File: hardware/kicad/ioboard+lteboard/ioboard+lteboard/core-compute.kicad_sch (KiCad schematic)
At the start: 14 parts, among them J7 USB_C_Receptacle_USB2.0_14P, J8 Amphenol_132163, SW1 SW_Push, SW2 SW_Push, U17 ESP32-S3-WROOM-1U

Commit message: Step 6: pin assignment and wiring on ioboard+lteboard
- core-compute: fix USB D+/D- to native GPIO19/GPIO20 (was on GPIO13/14)
- analog_io: expose ISO1540 logic-side I2C as hierarchical labels (bidirectional)
- core-compute: add 14 hierarchical labels for ethernet/lte/rs485/rs232 pin assignment
- root sheet: wire all 14 signals to their subsystems, confirm I2C 3-way merge
  (analog_io + core-compute + status_indication)
- root sheet: VBAT_LTE tied power<->lte (casual, ahead of the formal
  board-to-board connector decision, which stays a step 7 item; 3V3_LOGIC
  intentionally left split for the same reason)
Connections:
- net GND_LOGIC: now also R39.2; no longer R39.1
- net ETH_MISO: now reaches U17.21 (IO13)
- net ETH_MISO: no longer R40.1
- net at SW2.1: now also R39.1; no longer R39.2
- net ETH_INTN: now reaches U17.22 (IO14)
- net ETH_INTN: no longer R41.1
- net LTE_TXD: now reaches U17.10 (IO17)
- net LTE_RXD: now reaches U17.11 (IO18)
- net USB_D-: now reaches U17.13 (USB_D-)
- net USB_D-: now also R40.1
- net USB_D+: now reaches U17.14 (USB_D+)
- net USB_D+: now also R41.1
- net ETH_SCSN: now reaches U17.18 (IO10)
- net ETH_MOSI: now reaches U17.19 (IO11)
- net ETH_SCLK: now reaches U17.20 (IO12)
- net RS485_RXD: now reaches U17.38 (IO2)
- net RS485_TXD: now reaches U17.39 (IO1)
- net ETH_RSTN: now reaches U17.4 (IO4)
- net RS232_TXD: now reaches U17.5 (IO5)
- net RS232_RXD: now reaches U17.6 (IO6)
- net LTE_PWRKEY: now reaches U17.8 (IO15)
- net LTE_RESET: now reaches U17.9 (IO16)
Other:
- moved on the sheet: R39, R40, R41, SW2

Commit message: added missing hierarchical labels for core-compute, digitil_inputs and relay_output
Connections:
- net DI4_MCU: now reaches U17.15 (IO3)
- net DI7_MCU: now reaches U17.16 (IO46)
- net DI8_MCU: now reaches U17.24 (IO47)
- net DI3_MCU: now reaches U17.25 (IO48)
- net RELAY2_CTRL: now reaches U17.31 (IO38)
- net DI5_MCU: now reaches U17.32 (IO39)
- net DI1_MCU: now reaches U17.33 (IO40)
- net DI2_MCU: now reaches U17.34 (IO41)
- net DI6_MCU: now reaches U17.35 (IO42)
- net RELAY4_CTRL: now reaches U17.36 (RXD0)
- net RELAY3_CTRL: now reaches U17.37 (TXD0)
- net RELAY1_CTRL: now reaches U17.7 (IO7)
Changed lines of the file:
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@@
+		)
+	)
+	(hierarchical_label "DI7_MCU"
+		(shape input)
+		(at 144.78 100.33 0)
+		(effects
+			(font
+				(size 1.27 1.27)
+			)
+			(justify left)
 		)
 	)
@@
 		)
 	)
+	(hierarchical_label "DI6_MCU"
+		(shape input)
+		(at 144.78 95.25 0)
+		(effects
+			(font
+				(size 1.27 1.27)
+			)
+			(justify left)
+		)
+	)
+	(hierarchical_label "DI3_MCU"
+		(shape input)
+		(at 144.78 105.41 0)
+		(effects
+			(font
+				(size 1.27 1.27)
+			)
+			(justify left)
+		)
+	)
+	(hierarchical_label "RELAY4_CTRL"
+		(shape output)
+		(at 144.78 62.23 0)
+		(effects
+			(font
+				(size 1.27 1.27)
+			)
+			(justify left)
+		)
+	)
+	(hierarchical_label "DI8_MCU"
+		(shape input)
+		(at 144.78 102.87 0)
+		(effects
+			(font
+				(size 1.27 1.27)
+			)
+			(justify left)
+		)
+	)
+	(hierarchical_label "DI2_MCU"
+		(shape input)
+		(at 144.78 92.71 0)
+		(effects
+			(font
+				(size 1.27 1.27)
+			)
+			(justify left)
+		)
+	)
 	(hierarchical_label "LTE_RESET"
 		(shape output)
@@
 		)
 	)
+	(hierarchical_label "DI1_MCU"
+		(shape input)
+		(at 144.78 90.17 0)
+		(effects
+			(font
+				(size 1.27 1.27)
+			)
+			(justify left)
+		)
+	)
 	(hierarchical_label "ETH_RSTN"
 		(shape output)
@@
 		)
 	)
+	(hierarchical_label "RELAY2_CTRL"
+		(shape output)
+		(at 144.78 85.09 0)
+		(effects
+			(font
+				(size 1.27 1.27)
+			)
+			(justify left)
+		)
+	)
 	(hierarchical_label "ETH_SCSN"
 		(shape output)
@@
 		)
 	)
+	(hierarchical_label "DI5_MCU"
+		(shape input)
+		(at 144.78 87.63 0)
+		(effects
+			(font
+				(size 1.27 1.27)
+			)
+			(justify left)
+		)
+	)
 	(hierarchical_label "RS485_TXD"
 		(shape output)
@@
 		)
 	)
+	(hierarchical_label "DI4_MCU"
+		(shape input)
+		(at 114.3 72.39 180)
+		(effects
+			(font
+				(size 1.27 1.27)
+			)
+			(justify right)
+		)
+	)
 	(hierarchical_label "ETH_MOSI"
 		(shape output)
@@
 		)
 	)
+	(hierarchical_label "RELAY1_CTRL"
+		(shape output)
+		(at 114.3 82.55 180)
+		(effects
+			(font
+				(size 1.27 1.27)
+			)
+			(justify right)
+		)
+	)
 	(hierarchical_label "RS232_RXD"
 		(shape input)
@@
 		)
 	)
+	(hierarchical_label "RELAY3_CTRL"
+		(shape output)
+		(at 144.78 59.69 0)
+		(effects
+			(font
+				(size 1.27 1.27)
+			)
+			(justify left)
+		)
+	)

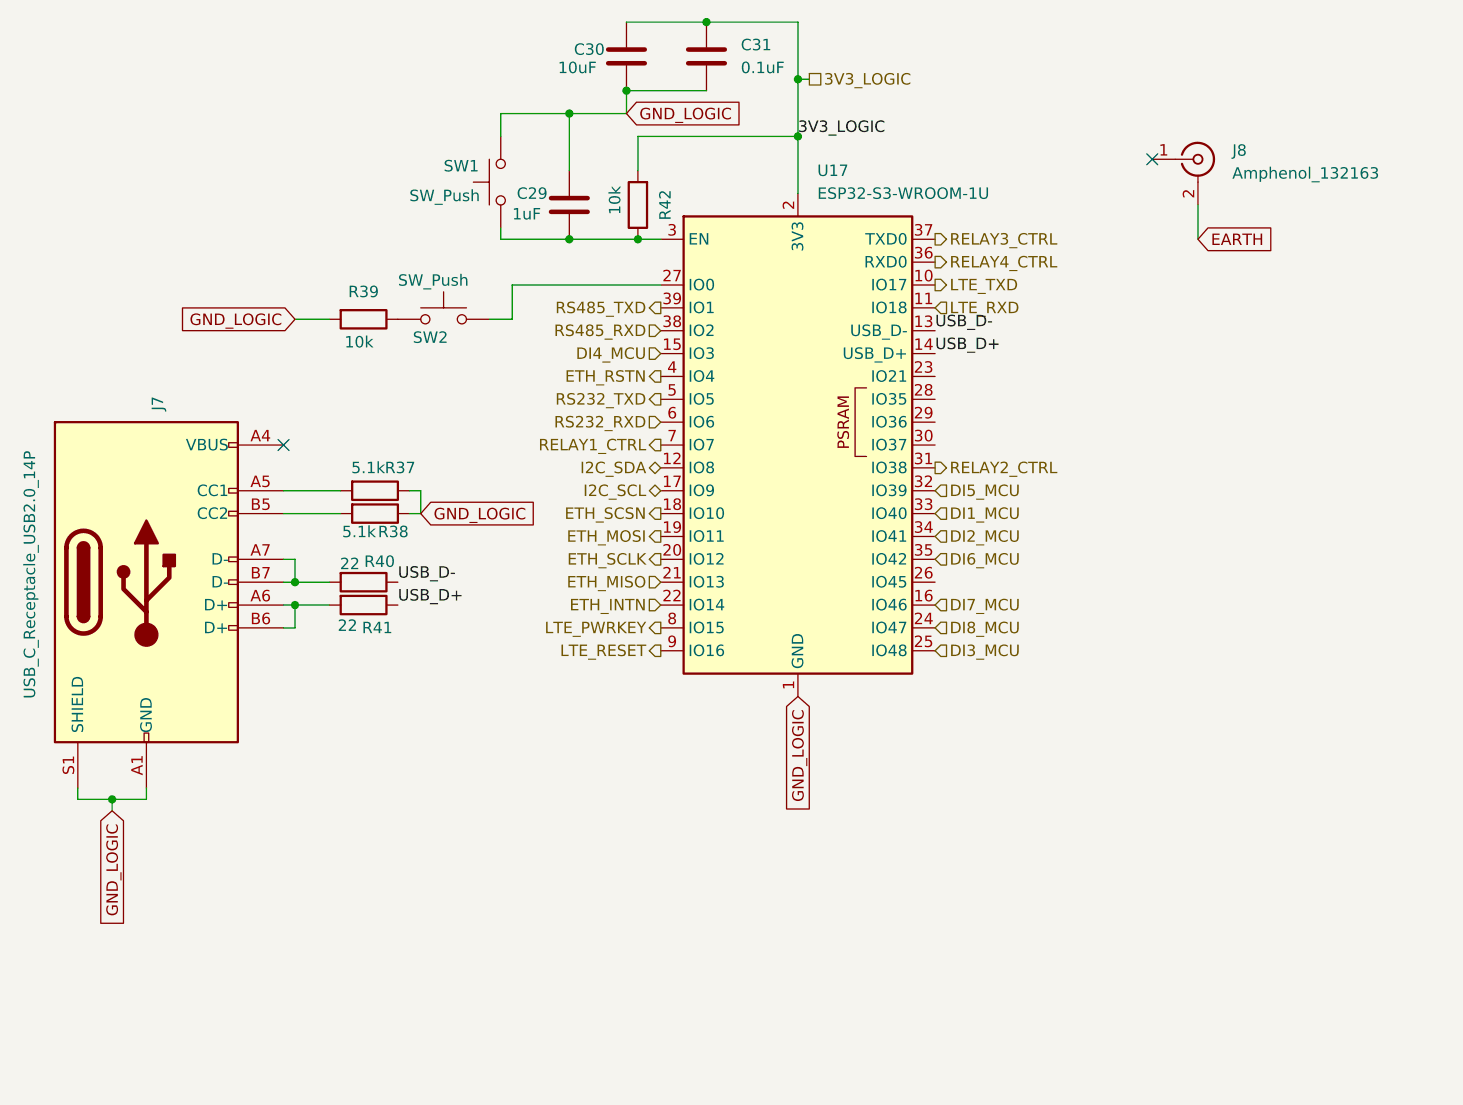
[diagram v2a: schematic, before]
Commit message: Close roadmap steps 6/7: pin assignment, board-to-board wiring, ERC pass clean; update docs to match
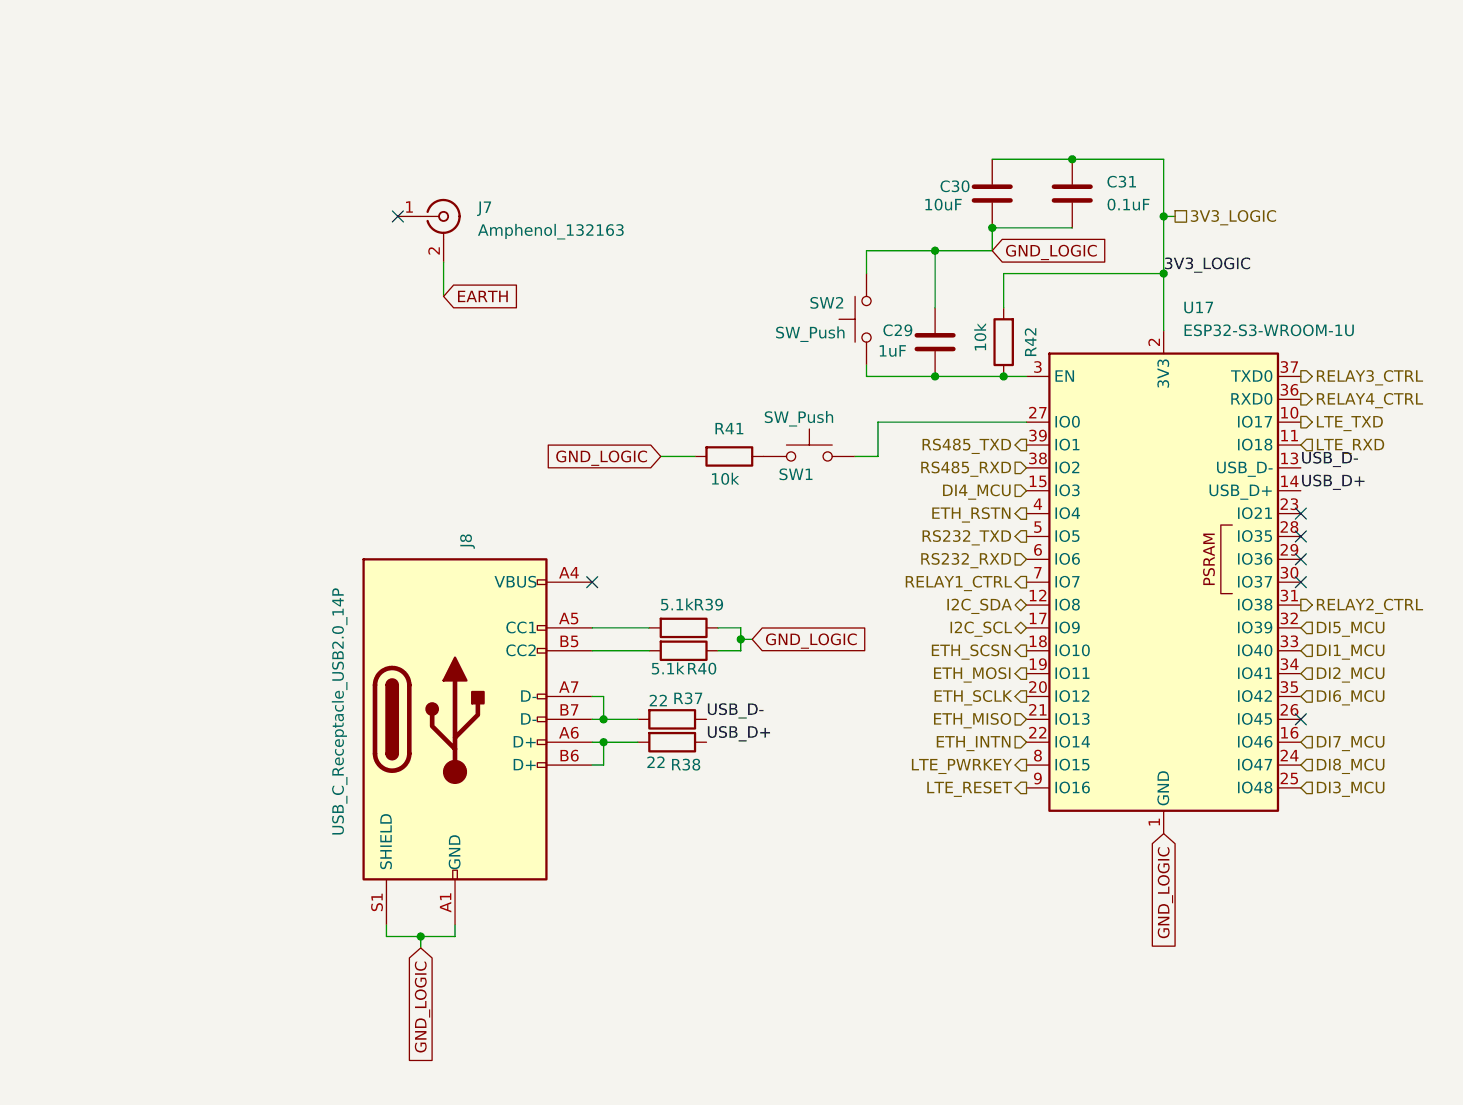
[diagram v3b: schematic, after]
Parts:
- renumbered J8 to J7, J7 to J8, R40 to R37, R41 to R38, R37 to R39, R38 to R40, R39 to R41, SW2 to SW1, SW1 to SW2
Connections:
- no-connect marks 2 -> 7
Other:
- moved on the sheet: C29, C30, C31, J7, J8, R37, R38, R39, R40, R41, R42, SW1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
